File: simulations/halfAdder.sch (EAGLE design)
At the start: 8 parts

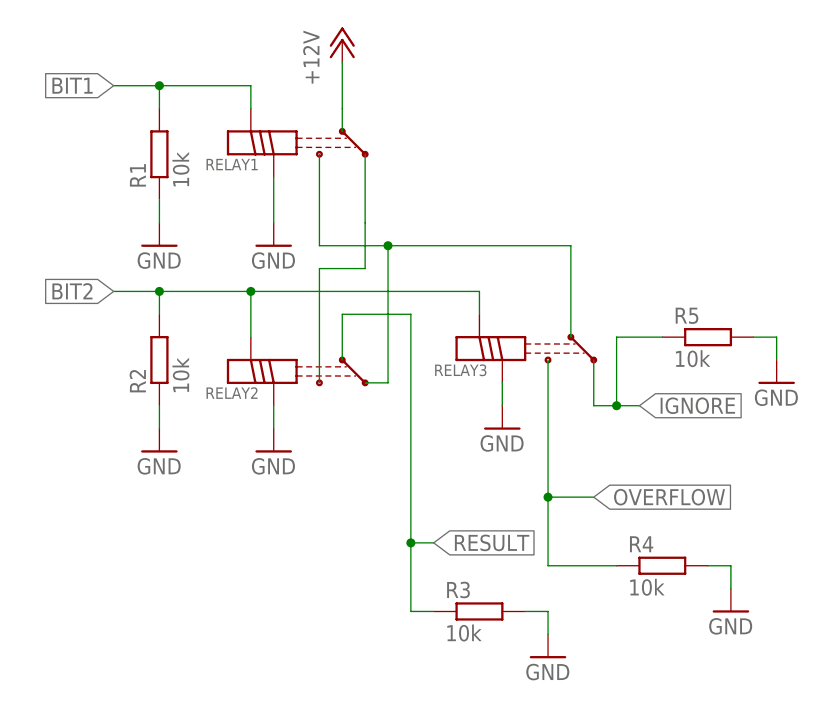
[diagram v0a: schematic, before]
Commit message: Refactoring relay module to include pull-downs
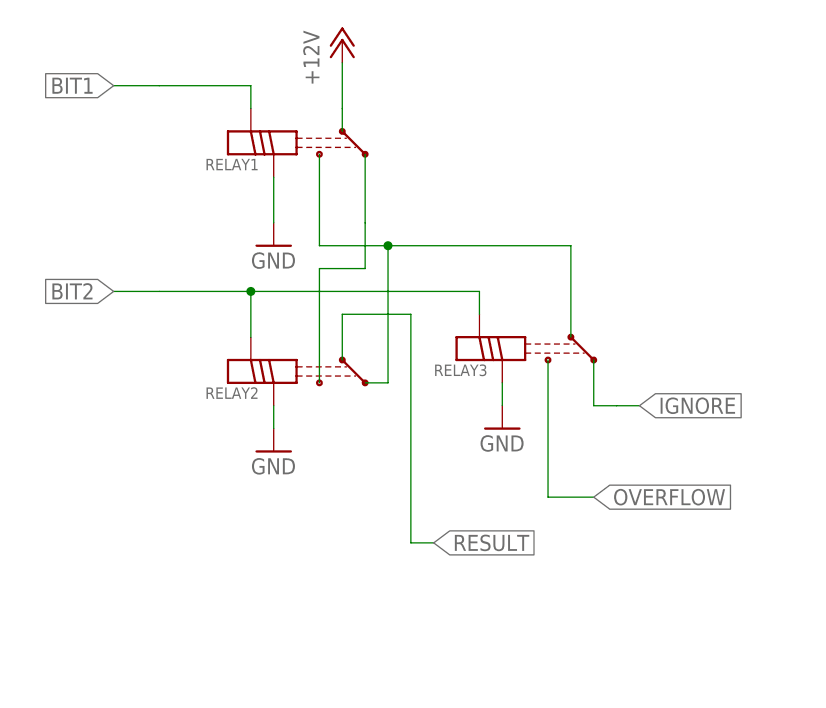
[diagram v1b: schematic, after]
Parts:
- removed R1, R2, R3, R4, R5: 10k, p.peter-scoville.tests:R-EU_R0603
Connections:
- net BIT1: no longer R1.2
- net BIT2: no longer R2.2
- net GND: no longer R1.1, R2.1, R3.2, R4.2, R5.2
- net IGNORE: no longer R5.1
- net OVERFLOW: no longer R4.1
- net RESULT: no longer R3.1
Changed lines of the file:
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@@
 <part name="GND2" library="supply1" deviceset="GND" device=""/>
 <part name="GND3" library="supply1" deviceset="GND" device=""/>
-<part name="R1" library="p.peter-scoville.tests" deviceset="R-EU_" device="R0603" value="10k"/>
-<part name="R2" library="p.peter-scoville.tests" deviceset="R-EU_" device="R0603" value="10k"/>
-<part name="R3" library="p.peter-scoville.tests" deviceset="R-EU_" device="R0603" value="10k"/>
-<part name="R4" library="p.peter-scoville.tests" deviceset="R-EU_" device="R0603" value="10k"/>
-<part name="R5" library="p.peter-scoville.tests" deviceset="R-EU_" device="R0603" value="10k"/>
-<part name="GND4" library="supply1" deviceset="GND" device=""/>
-<part name="GND5" library="supply1" deviceset="GND" device=""/>
-<part name="GND6" library="supply1" deviceset="GND" device=""/>
-<part name="GND7" library="supply1" deviceset="GND" device=""/>
-<part name="GND8" library="supply1" deviceset="GND" device=""/>
 </parts>
 <sheets>
@@
 <instance part="GND2" gate="1" x="50.8" y="7.62"/>
 <instance part="GND3" gate="1" x="76.2" y="10.16"/>
-<instance part="R1" gate="G$1" x="38.1" y="40.64" rot="R90"/>
-<instance part="R2" gate="G$1" x="38.1" y="17.78" rot="R90"/>
-<instance part="R3" gate="G$1" x="73.66" y="-10.16"/>
-<instance part="R4" gate="G$1" x="93.98" y="-5.08"/>
-<instance part="R5" gate="G$1" x="99.06" y="20.32"/>
-<instance part="GND4" gate="1" x="38.1" y="30.48"/>
-<instance part="GND5" gate="1" x="38.1" y="7.62"/>
-<instance part="GND6" gate="1" x="106.68" y="15.24"/>
-<instance part="GND7" gate="1" x="101.6" y="-10.16"/>
-<instance part="GND8" gate="1" x="81.28" y="-15.24"/>
 </instances>
 <busses>
@@
 <pinref part="RELAY1" gate="G$1" pin="N-"/>
 </segment>
-<segment>
-<pinref part="R1" gate="G$1" pin="1"/>
-<pinref part="GND4" gate="1" pin="GND"/>
-<wire x1="38.1" y1="33.02" x2="38.1" y2="35.56" width="0.1524" layer="91"/>
-</segment>
-<segment>
-<pinref part="R2" gate="G$1" pin="1"/>
-<pinref part="GND5" gate="1" pin="GND"/>
-<wire x1="38.1" y1="10.16" x2="38.1" y2="12.7" width="0.1524" layer="91"/>
-</segment>
-<segment>
-<pinref part="R5" gate="G$1" pin="2"/>
-<pinref part="GND6" gate="1" pin="GND"/>
-<wire x1="106.68" y1="17.78" x2="106.68" y2="20.32" width="0.1524" layer="91"/>
-<wire x1="106.68" y1="20.32" x2="104.14" y2="20.32" width="0.1524" layer="91"/>
-</segment>
-<segment>
-<pinref part="R4" gate="G$1" pin="2"/>
-<pinref part="GND7" gate="1" pin="GND"/>
-<wire x1="101.6" y1="-7.62" x2="101.6" y2="-5.08" width="0.1524" layer="91"/>
-<wire x1="101.6" y1="-5.08" x2="99.06" y2="-5.08" width="0.1524" layer="91"/>
-</segment>
-<segment>
-<pinref part="R3" gate="G$1" pin="2"/>
-<pinref part="GND8" gate="1" pin="GND"/>
-<wire x1="81.28" y1="-12.7" x2="81.28" y2="-10.16" width="0.1524" layer="91"/>
-<wire x1="81.28" y1="-10.16" x2="78.74" y2="-10.16" width="0.1524" layer="91"/>
-</segment>
 </net>
 <net name="+12V" class="0">
@@
 <wire x1="48.26" y1="48.26" x2="38.1" y2="48.26" width="0.1524" layer="91"/>
 <label x="33.02" y="48.26" size="1.778" layer="95" rot="R180" xref="yes"/>
-<pinref part="R1" gate="G$1" pin="2"/>
 <wire x1="38.1" y1="48.26" x2="33.02" y2="48.26" width="0.1524" layer="91"/>
-<wire x1="38.1" y1="48.26" x2="38.1" y2="45.72" width="0.1524" layer="91"/>
-<junction x="38.1" y="48.26"/>
 </segment>
 </net>
@@
 <wire x1="81.28" y1="2.54" x2="86.36" y2="2.54" width="0.1524" layer="91"/>
 <label x="86.36" y="2.54" size="1.778" layer="95" xref="yes"/>
-<pinref part="R4" gate="G$1" pin="1"/>
-<wire x1="88.9" y1="-5.08" x2="81.28" y2="-5.08" width="0.1524" layer="91"/>
-<wire x1="81.28" y1="-5.08" x2="81.28" y2="2.54" width="0.1524" layer="91"/>
-<junction x="81.28" y="2.54"/>
 </segment>
 </net>
@@
 <pinref part="RELAY3" gate="G$1" pin="N+"/>
 <junction x="48.26" y="25.4"/>
-<pinref part="R2" gate="G$1" pin="2"/>
-<wire x1="38.1" y1="22.86" x2="38.1" y2="25.4" width="0.1524" layer="91"/>
-<junction x="38.1" y="25.4"/>
 </segment>
 </net>
@@
 <wire x1="66.04" y1="-2.54" x2="68.58" y2="-2.54" width="0.1524" layer="91"/>
 <label x="68.58" y="-2.54" size="1.778" layer="95" xref="yes"/>
-<pinref part="R3" gate="G$1" pin="1"/>
-<wire x1="68.58" y1="-10.16" x2="66.04" y2="-10.16" width="0.1524" layer="91"/>
-<wire x1="66.04" y1="-10.16" x2="66.04" y2="-2.54" width="0.1524" layer="91"/>
-<junction x="66.04" y="-2.54"/>
 </segment>
 </net>
@@
 <wire x1="86.36" y1="12.7" x2="88.9" y2="12.7" width="0.1524" layer="91"/>
 <label x="91.44" y="12.7" size="1.778" layer="95" xref="yes"/>
-<pinref part="R5" gate="G$1" pin="1"/>
 <wire x1="88.9" y1="12.7" x2="91.44" y2="12.7" width="0.1524" layer="91"/>
-<wire x1="93.98" y1="20.32" x2="88.9" y2="20.32" width="0.1524" layer="91"/>
-<wire x1="88.9" y1="20.32" x2="88.9" y2="12.7" width="0.1524" layer="91"/>
-<junction x="88.9" y="12.7"/>
 </segment>
 </net>
